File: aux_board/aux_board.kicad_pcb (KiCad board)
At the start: 4 copper layers, 80 x 80 mm, 128 parts, among them J1 Conn_02x01, J10 Conn_01x03_Pin, J11 Conn_01x03_Pin, J2 Conn_02x13_Odd_Even, J3 Conn_02x01, J4 Conn_02x04_Odd_Even, J5 Conn_01x02_Pin, J6 Conn_02x24_Odd_Even, J7 10155435-00011LF, J8 10155435-00011LF, J9 10155435-00011LF, SW1 EVP-AA602W, SW3 EVP-AA602W, U1 AP63200WU, U10 FT230XS, U11 FT230XS, U2 AP63200WU, U3 AP63200WU, U4 AP63200WU, U5 STM32L496RGTx, U6 TJA1042TK-3, U7 TJA1042TK-3, Y1 8MHz

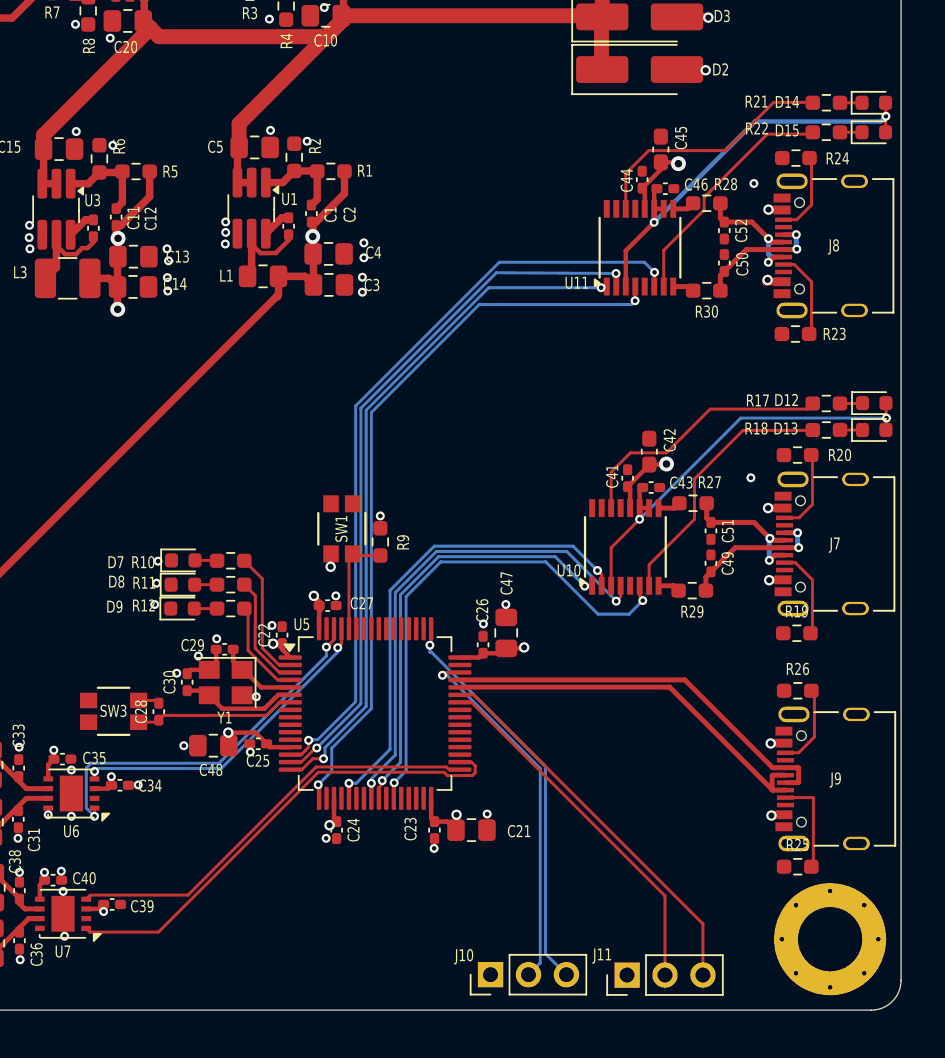
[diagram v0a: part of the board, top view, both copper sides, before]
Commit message: starting the SCI board with triple camera multiplexing
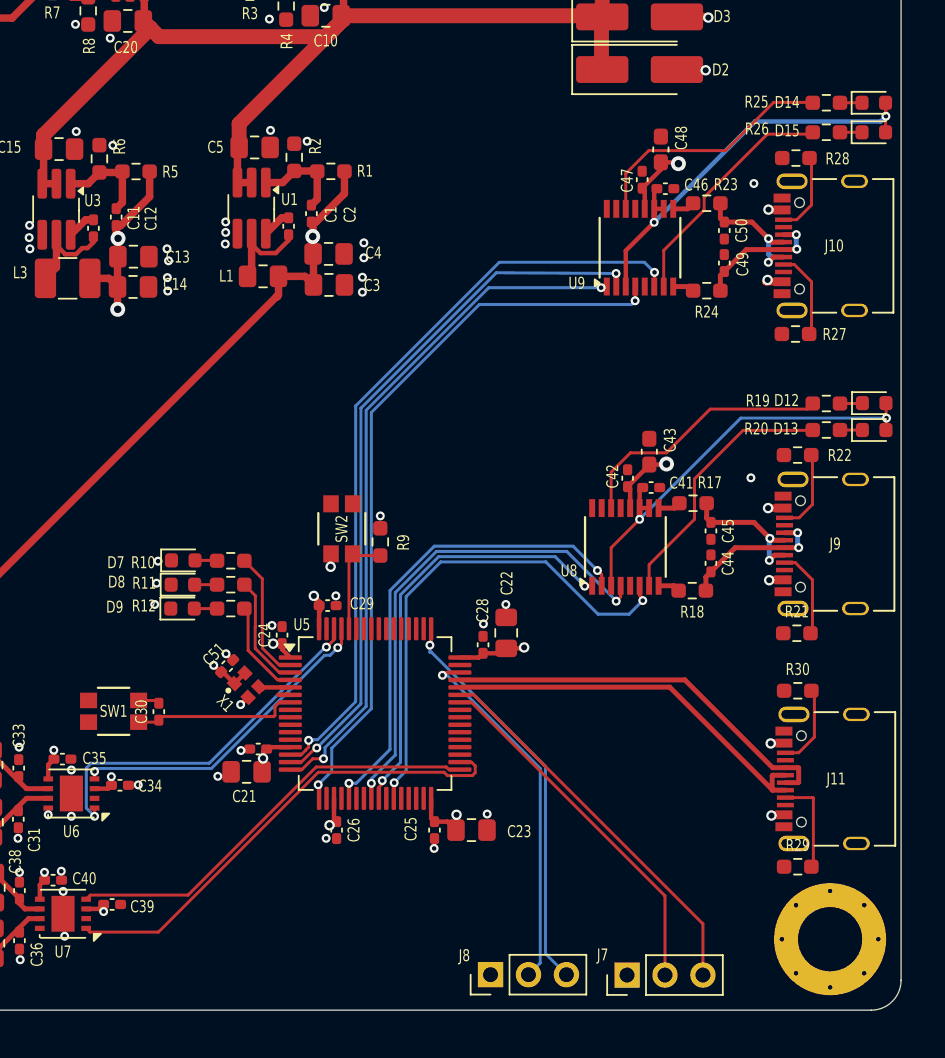
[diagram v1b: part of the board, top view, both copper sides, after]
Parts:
- removed the C29 at (94.7, 115.8)
- removed the C30 at (92.2, 118.0)
- removed Y1: 8MHz, Crystal:Crystal_SMD_3225-4Pin_3.2x2.5mm
- added C51: 100n, Capacitor_SMD:C_0402_1005Metric_Pad0.74x0.62mm_HandSolder, F.Cu at (94.9, 117.0)
- added X1: ECS-TXO-2016, Project:OSC_ECS-1618-300-BN-TR, F.Cu at (96.2, 118.2)
- moved C21 2.83 mm to (96.2, 124.0)
- moved C27 0.35 mm to (97.0, 122.5)
- renumbered C48 to C21, C47 to C22, C21 to C23, C22 to C24, C23 to C25, C24 to C26, C25 to C27, C26 to C28, C27 to C29, C28 to C30, C43 to C41, C41 to C42, C42 to C43, C49 to C44, C51 to C45, C44 to C47, C45 to C48, C50 to C49, C52 to C50, J8 to J10, J9 to J11, J11 to J7, J10 to J8, J7 to J9, R27 to R17, R29 to R18, R17 to R19, R18 to R20, R19 to R21, R20 to R22, R28 to R23, R30 to R24, R21 to R25, R22 to R26, R23 to R27, R24 to R28, R25 to R29, R26 to R30, SW3 to SW1, SW1 to SW2, U10 to U8, U11 to U9
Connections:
- U5 pad 6: /CAN TO USB/HSE_OUT -> unconnected-(U5-PH1-Pad6)
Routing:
- net /CAN TO USB/HSE_OUT: track 7.34 -> 0.00 mm
- net /CAN TO USB/HSE_IN: track 5.24 -> 2.44 mm
- net GND: track 4.32 -> 2.53 mm, vias 67 -> 65
- net unconnected-(U5-PH1-Pad6): track 0.00 -> 0.81 mm
- net +3V3: track 37.8 -> 38.3 mm, vias 11 -> 12

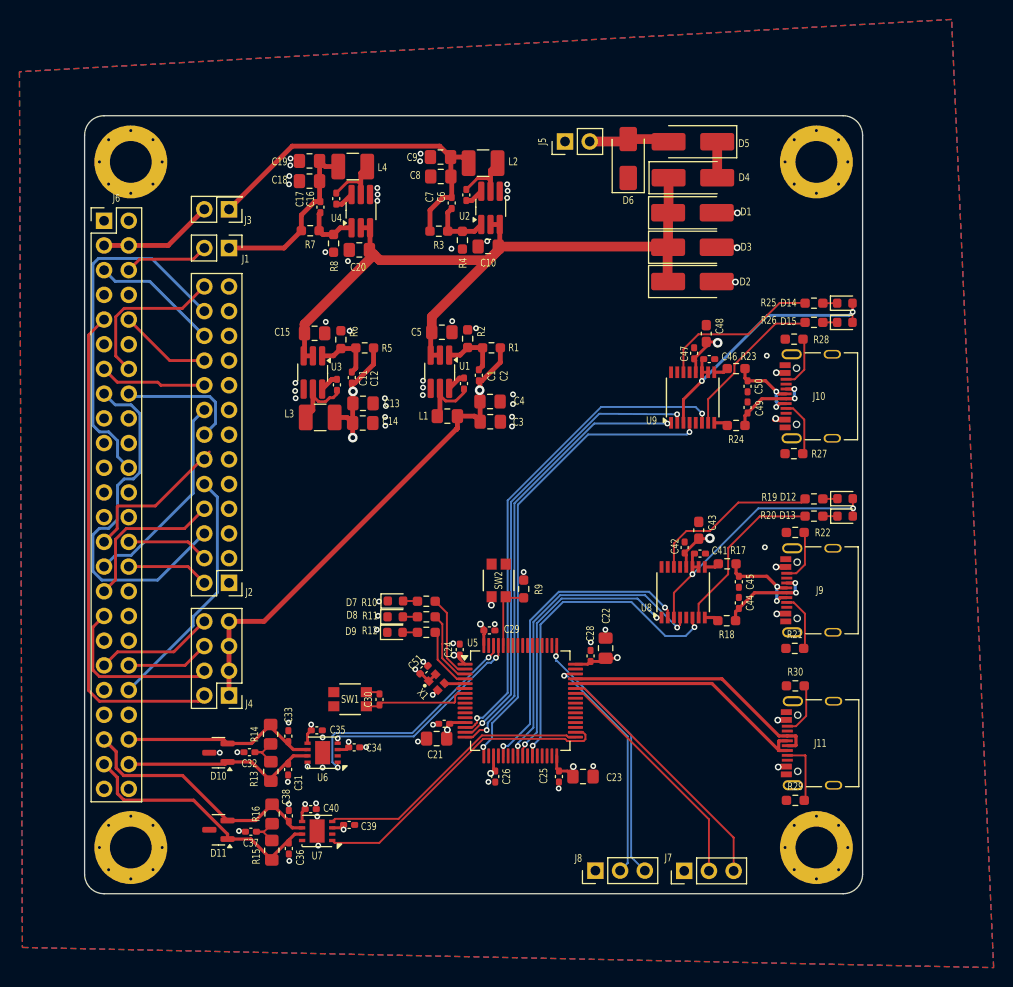
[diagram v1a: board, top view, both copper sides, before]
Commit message: replace nearly all buck converters with boost buck (missing is 5raw
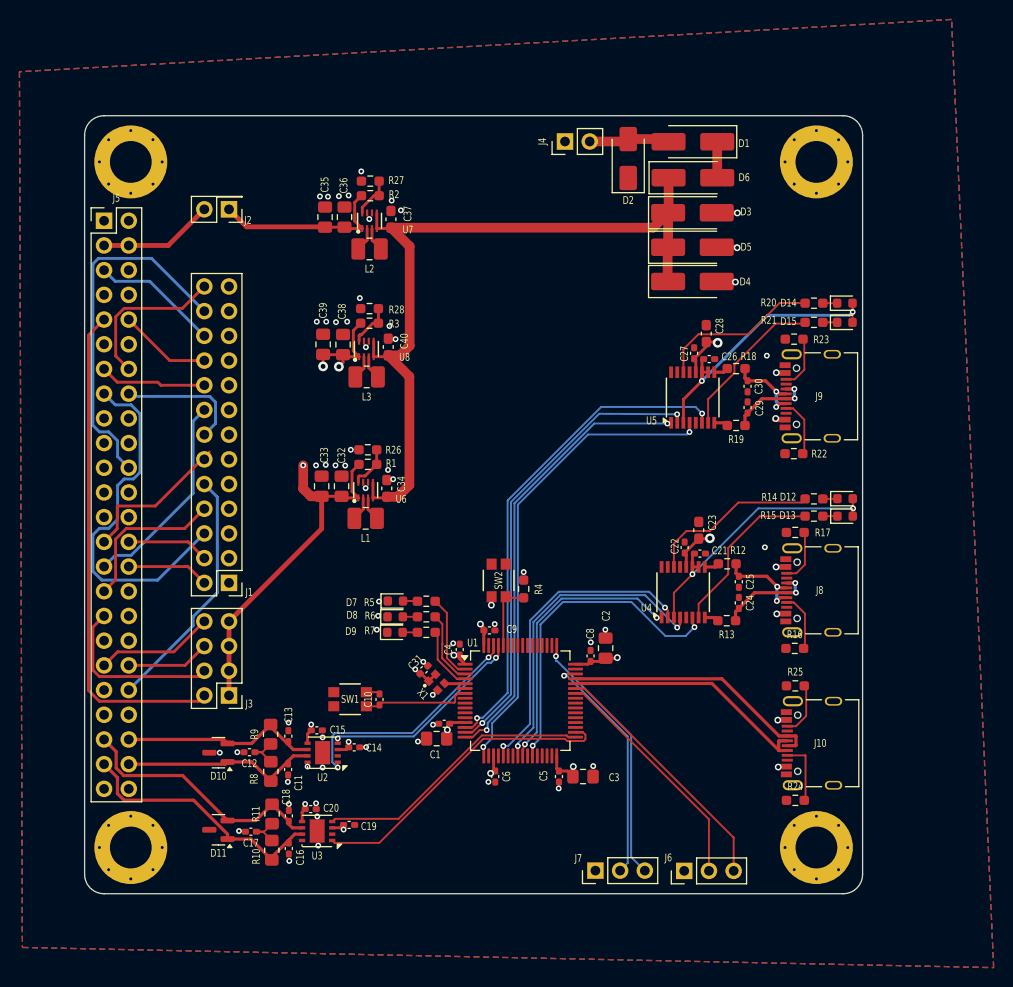
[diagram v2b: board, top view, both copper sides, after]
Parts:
- removed the C1 at (99.0, 87.5)
- removed the C10 at (101.5, 73.5)
- removed the C11 at (86.0, 87.7)
- removed the C12 at (87.5, 86.9)
- removed the C13 at (88.6, 89.6)
- removed the C14 at (88.6, 91.6)
- removed the C15 at (83.7, 82.4)
- removed the C16 at (85.9, 68.5)
- removed the C17 at (84.2, 69.4)
- removed the C18 at (83.1, 66.7)
- removed the C19 at (83.1, 64.7)
- removed the C2 at (100.5, 86.7)
- removed the C20 at (88.2, 73.8)
- removed the C3 at (101.7, 91.5)
- removed the C4 at (101.7, 89.4)
- removed the C5 at (96.7, 82.3)
- removed the C6 at (99.2, 68.2)
- removed the C7 at (97.8, 69.0)
- removed the C8 at (96.6, 66.2)
- removed the C9 at (96.6, 64.2)
- removed the J1 at (74.8, 73.6)
- removed L4: 3u3, Inductor_SMD:L_1210_3225Metric_Pad1.42x2.65mm_HandSolder
- removed the R4 at (98.8, 72.8)
- removed the R5 at (88.8, 83.9)
- removed the R6 at (86.3, 83.0)
- removed the R7 at (83.2, 71.8)
- removed the R8 at (85.6, 73.1)
- removed the U1 at (96.5, 86.3)
- removed the U2 at (101.7, 69.5)
- removed the U3 at (83.5, 86.4)
- removed the U4 at (88.4, 69.8)
- added C32: 47u, Capacitor_SMD:C_0805_2012Metric_Pad1.18x1.45mm_HandSolder, F.Cu at (86.4, 98.1)
- added C33: 47u, Capacitor_SMD:C_0805_2012Metric_Pad1.18x1.45mm_HandSolder, F.Cu at (84.4, 98.1)
- added C34: 22u, Capacitor_SMD:C_0603_1608Metric_Pad1.08x0.95mm_HandSolder, F.Cu at (91.1, 98.3)
- added C35: 47u, Capacitor_SMD:C_0805_2012Metric_Pad1.18x1.45mm_HandSolder, F.Cu at (84.7, 70.4)
- added C36: 47u, Capacitor_SMD:C_0805_2012Metric_Pad1.18x1.45mm_HandSolder, F.Cu at (86.7, 70.4)
- added C37: 22u, Capacitor_SMD:C_0603_1608Metric_Pad1.08x0.95mm_HandSolder, F.Cu at (91.5, 70.7)
- added C38: 47u, Capacitor_SMD:C_0805_2012Metric_Pad1.18x1.45mm_HandSolder, F.Cu at (86.6, 83.5)
- added C39: 47u, Capacitor_SMD:C_0805_2012Metric_Pad1.18x1.45mm_HandSolder, F.Cu at (84.5, 83.5)
- added C40: 22u, Capacitor_SMD:C_0603_1608Metric_Pad1.08x0.95mm_HandSolder, F.Cu at (91.2, 83.8)
- added R26: 91K, Resistor_SMD:R_0603_1608Metric_Pad0.98x0.95mm_HandSolder, F.Cu at (89.1, 94.3)
- added R27: 91K, Resistor_SMD:R_0603_1608Metric_Pad0.98x0.95mm_HandSolder, F.Cu at (89.4, 66.7)
- added R28: 91K, Resistor_SMD:R_0603_1608Metric_Pad0.98x0.95mm_HandSolder, F.Cu at (89.3, 79.8)
- added U6: TPS631000DRLR, Project:TPS631000DRLR_TEX, F.Cu at (88.9, 98.5)
- added U7: TPS631000DRLR, Project:TPS631000DRLR_TEX, F.Cu at (89.3, 70.8)
- added U8: TPS631000DRLR, Project:TPS631000DRLR_TEX, F.Cu at (89.0, 84.0)
- L1: value 10u -> 1u; footprint Capacitor_SMD:C_0805_2012Metric_Pad1.18x1.45mm_HandSolder -> Inductor_SMD:L_1008_2520Metric_Pad1.43x2.20mm_HandSolder
- L2: value 8u4 -> 1u; footprint Inductor_SMD:L_1210_3225Metric_Pad1.42x2.65mm_HandSolder -> Inductor_SMD:L_1008_2520Metric_Pad1.43x2.20mm_HandSolder
- L3: value 3u3 -> 1u; footprint Inductor_SMD:L_1210_3225Metric_Pad1.42x2.65mm_HandSolder -> Inductor_SMD:L_1008_2520Metric_Pad1.43x2.20mm_HandSolder
- R1: value 157K -> 806K
- R2: value 30K -> 673K4
- R3: value 182K -> 511K
- X1: value ECS-TXO-2016 -> ECS-TXO-2016-33-100-TR
- moved R2 17.8 mm to (89.4, 68.2), turned to 180 degrees
- moved R1 17.5 mm to (89.1, 95.8), turned to 180 degrees
- moved L2 14.6 mm to (89.3, 73.7)
- moved L1 13.5 mm to (88.9, 101.4), turned to 180 degrees
- moved R3 11.8 mm to (89.3, 81.3)
- moved L3 6.34 mm to (89.0, 86.9), turned to 180 degrees
- renumbered C21 to C1, C30 to C10, C31 to C11, C32 to C12, C33 to C13, C34 to C14, C35 to C15, C36 to C16, C37 to C17, C38 to C18, C39 to C19, C22 to C2, C40 to C20, C41 to C21, C42 to C22, C43 to C23, C44 to C24, C45 to C25, C46 to C26, C47 to C27, C48 to C28, C49 to C29, C23 to C3, C50 to C30, C51 to C31, C24 to C4, C25 to C5, C26 to C6, C27 to C7, C28 to C8, C29 to C9, D5 to D1, D6 to D2, D1 to D3, D2 to D4, D3 to D5, D4 to D6, J2 to J1, J11 to J10, J3 to J2, J4 to J3, J5 to J4, J6 to J5, J7 to J6, J8 to J7, J9 to J8, J10 to J9, R15 to R10, R16 to R11, R17 to R12, R18 to R13, R19 to R14, R20 to R15, R21 to R16, R22 to R17, R23 to R18, R24 to R19, R25 to R20, R26 to R21, R27 to R22, R28 to R23, R29 to R24, R30 to R25, R9 to R4, R10 to R5, R11 to R6, R12 to R7, R13 to R8, R14 to R9, U5 to U1, U6 to U2, U7 to U3, U8 to U4, U9 to U5
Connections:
- J2 pad 1: +4V2 -> +VBAT
- L1 pad 1: /Regulator/L+ -> /Regulator 5V/LX1
- L1 pad 2: +5V -> /Regulator 5V/LX2
- L2 pad 1: /Regulator1/L+ -> /Regulator 4V2/LX1
- L2 pad 2: +4V2 -> /Regulator 4V2/LX2
- L3 pad 1: /Regulator2/L+ -> /Regulator 3V3/LX1
- L3 pad 2: +3V3 -> /Regulator 3V3/LX2
- R1 pad 1: /Regulator/R1- -> /Regulator 5V/R-
- R2 pad 1: /Regulator/R1- -> /Regulator 4V2/R-
- R2 pad 2: GND -> +VBAT
- R3 pad 1: /Regulator1/R1- -> /Regulator 3V3/R-
- R3 pad 2: +4V2 -> +3V3
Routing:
- net +4V2: track 37.0 -> 0.00 mm
- net +2V8: track 18.7 -> 0.00 mm
- net +VBAT: track 0.00 -> 18.5 mm
- net /INTERBOARD_CONNECTOR/2V8_1: track 8.70 -> 0.00 mm
- net +5V: track 138.2 -> 145.6 mm
- net /Regulator3/L+: track 7.30 -> 0.00 mm
- net /Regulator1/L+: track 7.26 -> 0.00 mm
- net /Regulator2/L+: track 6.64 -> 0.00 mm
- net /Regulator2/R1-: track 6.37 -> 0.00 mm
- net /Regulator1/R1-: track 6.23 -> 0.00 mm
- net /Regulator/R1-: track 6.15 -> 0.00 mm
- net /Regulator/L+: track 6.02 -> 0.00 mm
- net /Regulator3/R1-: track 5.70 -> 0.00 mm
- net /Regulator 3V3/R-: track 0.00 -> 4.59 mm
- net /Regulator 5V/R-: track 0.00 -> 4.49 mm
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
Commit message: AUX to PCI104
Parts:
- D2: value SMAJ12CA -> SMAJ6.0CA; footprint Diode_SMD:D_SMA -> Diode_SMD:D_SMA_Handsoldering
- J2: value Conn_02x01 -> Conn_02x03_Odd_Even; footprint Connector_PinHeader_2.54mm:PinHeader_2x01_P2.54mm_Vertical -> Connector_PinHeader_2.54mm:PinHeader_2x03_P2.54mm_Vertical
- J5: value Conn_02x24_Odd_Even -> PC104 Conn_02x20_Odd_Even; footprint Connector_PinHeader_2.54mm:PinHeader_2x24_P2.54mm_Vertical -> Connector_PinSocket_2.54mm:PinSocket_2x20_P2.54mm_Vertical
- R26, R27, R28: footprint Resistor_SMD:R_0603_1608Metric_Pad0.98x0.95mm_HandSolder -> Resistor_SMD:R_0402_1005Metric_Pad0.72x0.64mm_HandSolder
- moved J5 5.68 mm to (64.5, 75.9)
- moved J2 4.04 mm to (74.8, 73.7)
- moved D2 0.98 mm to (115.9, 65.4)
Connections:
- net /INTERBOARD_CONNECTOR/UART_B_CTS renamed /INTERBOARD_CONNECTOR/*SCI_RST
- net /INTERBOARD_CONNECTOR/UART_B_RXI renamed /INTERBOARD_CONNECTOR/*COMM2_RST
- net /INTERBOARD_CONNECTOR/UART_B_TXO renamed /INTERBOARD_CONNECTOR/*COMM1_RST
- J5 pad 10: /INTERBOARD_CONNECTOR/3V3_10 -> /INTERBOARD_CONNECTOR/3V3_12
- J5 pad 11: unconnected-(J5-Pin_11-Pad11) -> /INTERBOARD_CONNECTOR/3V3_11
- J5 pad 12: /INTERBOARD_CONNECTOR/EPS_RESET -> /INTERBOARD_CONNECTOR/3V3_10
- J5 pad 13: /INTERBOARD_CONNECTOR/3V3_9 -> /INTERBOARD_CONNECTOR/3V3_7
- J5 pad 14: /INTERBOARD_CONNECTOR/3V3_13 -> /INTERBOARD_CONNECTOR/3V3_6
- J5 pad 15: /INTERBOARD_CONNECTOR/3V3_3 -> /INTERBOARD_CONNECTOR/3V3_9
- J5 pad 16: /INTERBOARD_CONNECTOR/3V3_7 -> /INTERBOARD_CONNECTOR/3V3_8
- J5 pad 17: /INTERBOARD_CONNECTOR/UART_A_TXO -> /INTERBOARD_CONNECTOR/3V3_5
- J5 pad 18: /INTERBOARD_CONNECTOR/UART_A_RXI -> /INTERBOARD_CONNECTOR/3V3_4
- J5 pad 19: /INTERBOARD_CONNECTOR/UART_B_RTS -> /INTERBOARD_CONNECTOR/3V3_3
- J5 pad 20: /INTERBOARD_CONNECTOR/AVI_RESET -> /INTERBOARD_CONNECTOR/3V3_2
- J5 pad 21: GND -> /INTERBOARD_CONNECTOR/*ATTENTION
- J5 pad 22: /INTERBOARD_CONNECTOR/3V3_12 -> /INTERBOARD_CONNECTOR/*EPS_RST
- J5 pad 24: GND -> /INTERBOARD_CONNECTOR/*AVI_RST
- J5 pad 27: /INTERBOARD_CONNECTOR/3V3_6 -> GND
- J5 pad 28: /INTERBOARD_CONNECTOR/3V3_2 -> GND
- J5 pad 29: /INTERBOARD_CONNECTOR/3V3_8 -> /INTERBOARD_CONNECTOR/5V0_1
- J5 pad 3: /INTERBOARD_CONNECTOR/BATT -> /INTERBOARD_CONNECTOR/BATT_1
- J5 pad 30: /INTERBOARD_CONNECTOR/3V3_1 -> /INTERBOARD_CONNECTOR/5V0_2
- J5 pad 31: /INTERBOARD_CONNECTOR/3V3_4 -> /INTERBOARD_CONNECTOR/5V0_3
- J5 pad 32: GND -> /INTERBOARD_CONNECTOR/5V0_4
- J5 pad 33: /INTERBOARD_CONNECTOR/5V0_2 -> GND
- J5 pad 34: /INTERBOARD_CONNECTOR/SCI_RST -> GND
- J5 pad 35: GND -> /CAN2_L
- J5 pad 36: GND -> /CAN1_L
- J5 pad 37: /INTERBOARD_CONNECTOR/5V0_4 -> /CAN2_H
- J5 pad 38: /INTERBOARD_CONNECTOR/5V0_3 -> /CAN1_H
- J5 pad 39: unconnected-(J5-Pin_39-Pad39) -> GND
- J5 pad 4: /INTERBOARD_CONNECTOR/BATT -> /INTERBOARD_CONNECTOR/BATT_2
- J5 pad 40: /INTERBOARD_CONNECTOR/3V3_5 -> GND
- J5 pad 5: /INTERBOARD_CONNECTOR/3V3_11 -> GND
- J5 pad 6: /INTERBOARD_CONNECTOR/2V8_1 -> GND
- J5 pad 7: GND -> /INTERBOARD_CONNECTOR/3V3_1
- J5 pad 8: GND -> /INTERBOARD_CONNECTOR/BATT
- J5 pad 9: /INTERBOARD_CONNECTOR/5V0_1 -> /INTERBOARD_CONNECTOR/3V3_13
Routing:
- net /INTERBOARD_CONNECTOR/5V0_1: track 51.4 -> 18.4 mm
- net /INTERBOARD_CONNECTOR/3V3_1: track 8.46 -> 38.4 mm
- net /INTERBOARD_CONNECTOR/3V3_3: track 37.7 -> 9.55 mm
- net /INTERBOARD_CONNECTOR/3V3_12: track 37.0 -> 12.9 mm
- net /INTERBOARD_CONNECTOR/BATT_2: track 0.00 -> 18.0 mm
- net /INTERBOARD_CONNECTOR/3V3_5: track 25.5 -> 8.50 mm
- net /INTERBOARD_CONNECTOR/BATT_1: track 0.00 -> 10.8 mm
- net /INTERBOARD_CONNECTOR/3V3_8: track 21.3 -> 11.8 mm
- net /CAN1_H: track 20.3 -> 29.8 mm
- net /CAN1_L: track 20.3 -> 29.0 mm
- net +VBAT: track 18.5 -> 26.3 mm
- net /INTERBOARD_CONNECTOR/3V3_7: track 12.7 -> 17.4 mm
- net /INTERBOARD_CONNECTOR/3V3_2: track 8.46 -> 13.1 mm
- net /INTERBOARD_CONNECTOR/3V3_13: track 16.3 -> 11.9 mm
- net /INTERBOARD_CONNECTOR/3V3_4: track 16.3 -> 12.1 mm
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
